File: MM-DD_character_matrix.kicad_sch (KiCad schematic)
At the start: 17 parts, among them U10 SM411006N/15, U11 SN74LVC244A, U12 SM411006N/15, U13 SM411006N/15, U14 SM411006N/15, U8 SN74LVC244A, U9 SM411006N/15

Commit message: verification
- sensor schematic verification
- change in the value of current limiting resistor
- disconnected unused buffer pins
- labeling or peripherals used in primary MCU
- additional user button
- DRC corrections
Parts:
- R10, R44, R45, R46, R6, R7, R8, R9: value 20R -> 10R
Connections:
- net GND: no longer U11.5 (2Y1), U11.7 (2Y2), U11.9 (2Y3)
- no-connect marks 0 -> 3
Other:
- company: Rajath Katker -> TJ71PL
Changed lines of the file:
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@@
 	(title_block
 		(title "MM-DD Character Matrix & Drivers ")
-		(date "2025-11-04")
+		(date "2025-09-05")
 		(rev "v0.0")
-		(company "Rajath Katker")
+		(company "TJ71PL")
+		(comment 1 "天計")
 		(comment 4 "Final verification pending")
 	)
@@
 	(text "MM-DD Character matrix"
 		(exclude_from_sim no)
-		(at 17.78 95.25 0)
+		(at 16.51 96.52 0)
 		(effects
 			(font
@@
 	(text "MM-DD Character matrix drivers "
 		(exclude_from_sim no)
-		(at 16.51 191.77 0)
+		(at 15.24 193.548 0)
 		(effects
 			(font
@@
 	)
 	(junction
-		(at 161.29 152.4)
-		(diameter 0)
-		(color 0 0 0 0)
-	)
-	(junction
-		(at 161.29 154.94)
-		(diameter 0)
-		(color 0 0 0 0)
-	)
-	(junction
 		(at 130.81 152.4)
 		(diameter 0)
@@
 		(color 0 0 0 0)
 	)
+	(no_connect
+		(at 158.75 154.94)
+	)
+	(no_connect
+		(at 158.75 149.86)
+	)
+	(no_connect
+		(at 158.75 152.4)
+	)
 	(bus_entry
 		(at 168.91 134.62)
@@
 	(wire
 		(pts
-			(xy 161.29 149.86) (xy 161.29 152.4)
-		)
-		(stroke
-			(width 0)
-			(type default)
-		)
-	)
-	(wire
-		(pts
 			(xy 158.75 147.32) (xy 166.37 147.32)
 		)
@@
 		)
 	)
-	(wire
-		(pts
-			(xy 161.29 172.72) (xy 146.05 172.72)
-		)
-		(stroke
-			(width 0)
-			(type default)
-		)
-	)
 	(bus
 		(pts
@@
 	(wire
 		(pts
-			(xy 161.29 154.94) (xy 161.29 172.72)
-		)
-		(stroke
-			(width 0)
-			(type default)
-		)
-	)
-	(wire
-		(pts
 			(xy 130.81 152.4) (xy 133.35 152.4)
 		)
@@
 	(wire
 		(pts
-			(xy 158.75 154.94) (xy 161.29 154.94)
-		)
-		(stroke
-			(width 0)
-			(type default)
-		)
-	)
-	(wire
-		(pts
 			(xy 91.44 149.86) (xy 99.06 149.86)
 		)
@@
 		)
 	)
-	(wire
-		(pts
-			(xy 158.75 149.86) (xy 161.29 149.86)
-		)
-		(stroke
-			(width 0)
-			(type default)
-		)
-	)
 	(bus
 		(pts
@@
 		)
 	)
-	(wire
-		(pts
-			(xy 161.29 152.4) (xy 161.29 154.94)
-		)
-		(stroke
-			(width 0)
-			(type default)
-		)
-	)
 	(bus
 		(pts
@@
 		)
 	)
-	(wire
-		(pts
-			(xy 158.75 152.4) (xy 161.29 152.4)
-		)
-		(stroke
-			(width 0)
-			(type default)
-		)
-	)
 	(bus
 		(pts
@@
 			)
 		)
-		(property "Value" "20R"
+		(property "Value" "10R"
 			(at 87.63 170.434 90)
 			(effects
@@
 			)
 		)
-		(property "Value" "20R"
+		(property "Value" "10R"
 			(at 87.63 147.574 90)
 			(effects
@@
 			)
 		)
-		(property "Value" "20R"
+		(property "Value" "10R"
 			(at 87.63 162.814 90)
 			(effects
@@
 			)
 		)
-		(property "Value" "20R"
+		(property "Value" "10R"
 			(at 87.63 155.194 90)
 			(effects
@@
 			)
 		)
-		(property "Value" "20R"
+		(property "Value" "10R"
 			(at 87.63 117.094 90)
 			(effects
@@
 			)
 		)
-		(property "Value" "20R"
+		(property "Value" "10R"
 			(at 87.63 132.334 90)
 			(effects
@@
 			)
 		)
-		(property "Value" "20R"
+		(property "Value" "10R"
 			(at 87.63 124.714 90)
 			(effects
@@
 			)
 		)
-		(property "Value" "20R"
+		(property "Value" "10R"
 			(at 87.63 139.954 90)
 			(effects

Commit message: semi final verification
- change in display type to common cathode
- verification of the schematic
- addition of footprints
- further minor changes
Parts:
- removed U10, U12, U13, U14, U9: SM411006N/15, precision_clock:SM411006N15, symbol precision_clock:SM411006N/15
- added U10, U12, U13, U14, U9: 10016AS, precision_clock:10016AS, symbol precision_clock:10016AS
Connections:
- net BA0: now also R6.2, U10.7 (A), U12.7 (A), U14.7 (A), U9.7 (A); no longer U11.18 (1Y0)
- net BA1: now also R7.2, U10.6 (B), U12.6 (B), U13.6 (B), U13.7 (A), U14.6 (B), U9.6 (B); no longer U11.16 (1Y1)
- net BA2: now also R8.2, U10.4 (C), U12.4 (C), U13.4 (C), U14.4 (C), U9.4 (C); no longer U11.14 (1Y2)
- net BA3: now also R9.2, U10.2 (D), U12.2 (D), U13.2 (D), U14.2 (D), U9.2 (D); no longer U11.12 (1Y3)
- net BA4: now also R10.2, U10.1 (E), U12.1 (E), U13.1 (E), U14.1 (E), U9.1 (E); no longer U11.3 (2Y0)
- net BK0: now also U11.18 (1Y0), U9.3 (CK), U9.8 (CK); no longer R6.2
- net BK1: now also U11.16 (1Y1), U10.3 (CK), U10.8 (CK); no longer R7.2
- net BK2: now also U11.14 (1Y2), U12.3 (CK), U12.8 (CK); no longer R8.2
- net BK3: now also U11.12 (1Y3), U13.3 (CK), U13.8 (CK); no longer R9.2
- net BK4: now also U11.3 (2Y0), U14.3 (CK), U14.8 (CK); no longer R10.2
- net M2A0: now also U8.2 (1A0); no longer U11.2 (1A0)
- net M2A1: now also U8.4 (1A1); no longer U11.4 (1A1)
- net M2A2: now also U8.6 (1A2); no longer U11.6 (1A2)
- net M2A3: now also U8.8 (1A3); no longer U11.8 (1A3)
- net M2A4: now also U8.17 (2A0); no longer U11.17 (2A0)
- net M2K0: now also U11.2 (1A0); no longer U8.2 (1A0)
- net M2K1: now also U11.4 (1A1); no longer U8.4 (1A1)
- net M2K2: now also U11.6 (1A2); no longer U8.6 (1A2)
- net M2K3: now also U11.8 (1A3); no longer U8.8 (1A3)
- net M2K4: now also U11.17 (2A0); no longer U8.17 (2A0)
- net BK5 renamed BA5
- net BA5: now also U10.9 (F), U12.9 (F), U13.9 (F), U14.9 (F), U9.9 (F)
- net BK6 renamed BA6
- net BA6: now also U10.10 (G), U12.10 (G), U13.10 (G), U14.10 (G), U9.10 (G)
- net BK7 renamed BA7
- net BA7: now also U10.5 (DP), U12.5 (DP), U13.5 (DP), U14.5 (DP), U9.5 (DP)
- net M2K5 renamed M2A5
- net M2K6 renamed M2A6
- net M2K7 renamed M2A7

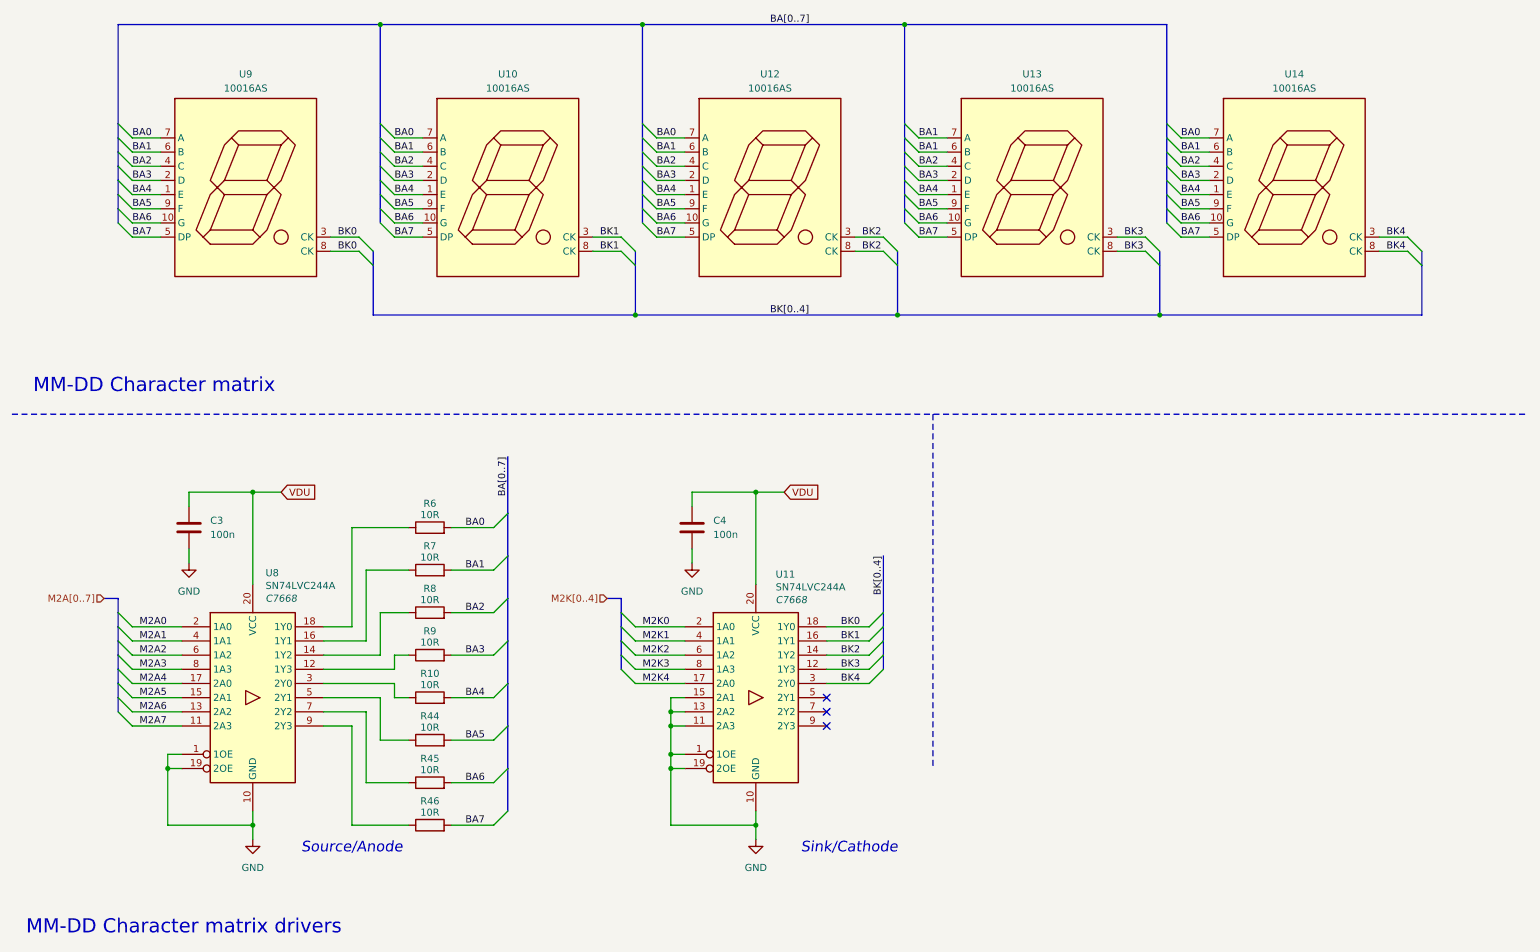
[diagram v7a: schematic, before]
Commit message: PCB routing
- JLCPCB constraints added
- removal of multiple test points
- change of footprints
- change of THT LEDs
- rough position of all the major components
- PCB routing started
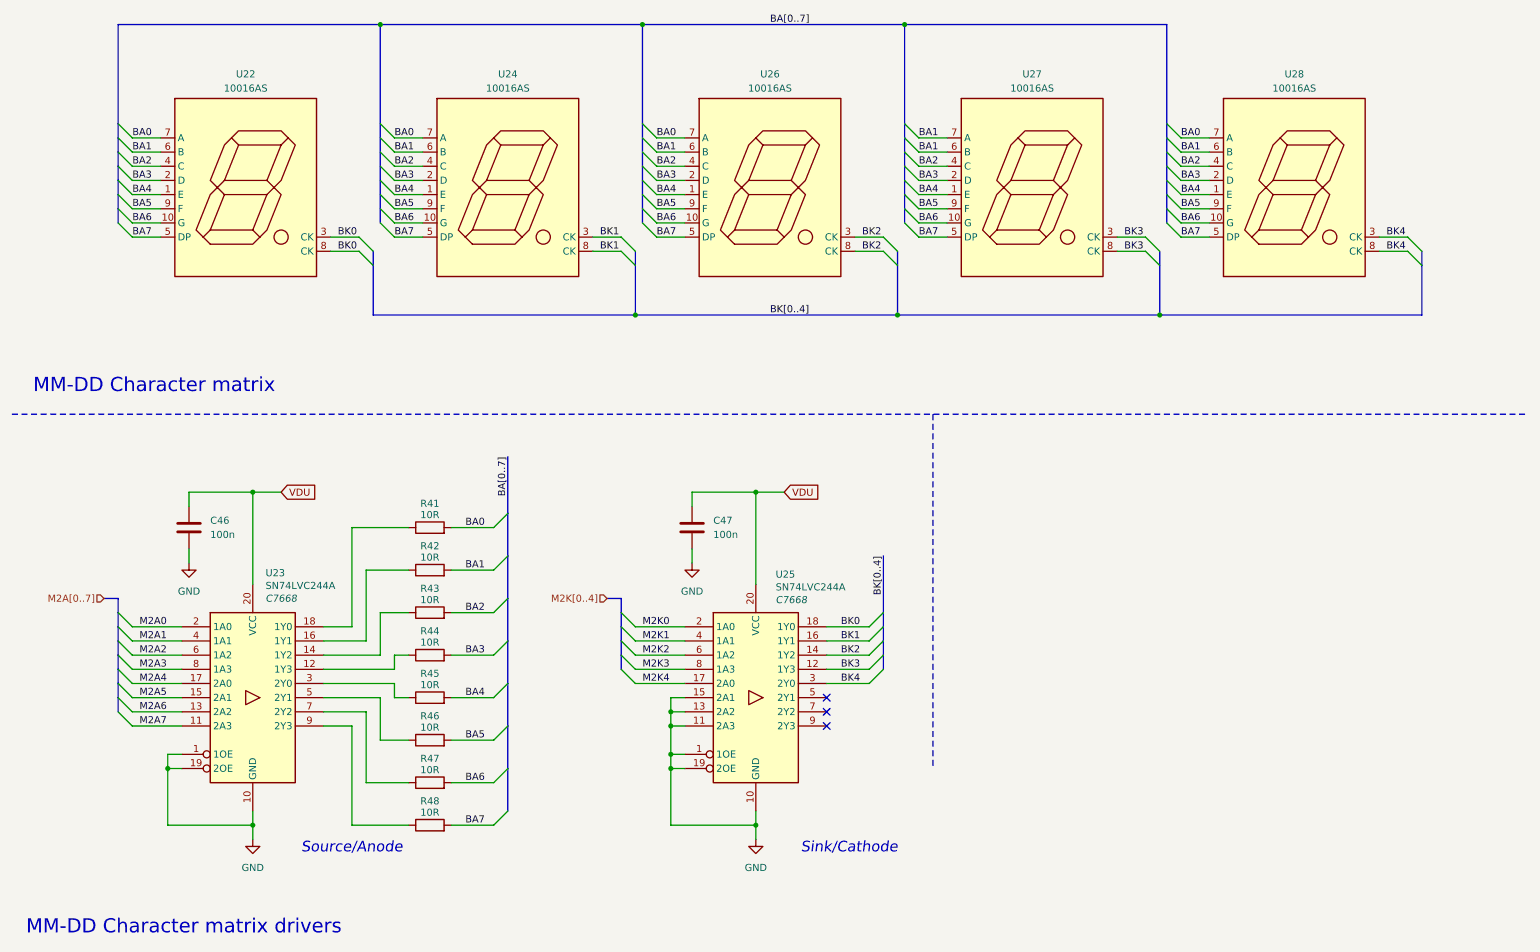
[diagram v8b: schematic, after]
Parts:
- U22: renamed from U9; footprint precision_clock:10016AS -> precision_clock:Xlitx 10016AS
- U24: renamed from U10; footprint precision_clock:10016AS -> precision_clock:Xlitx 10016AS
- U26: renamed from U12; footprint precision_clock:10016AS -> precision_clock:Xlitx 10016AS
- U27: renamed from U13; footprint precision_clock:10016AS -> precision_clock:Xlitx 10016AS
- U28: renamed from U14; footprint precision_clock:10016AS -> precision_clock:Xlitx 10016AS
- renumbered C3 to C46, C4 to C47, R6 to R41, R7 to R42, R8 to R43, R9 to R44, R10 to R45, R44 to R46, R45 to R47, R46 to R48, U8 to U23, U11 to U25
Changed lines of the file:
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@@
 		(on_board yes)
 		(dnp no)
-		(property "Reference" "U8"
+		(property "Reference" "U23"
 			(at 58.166 130.048 0)
 			(effects
@@
 			(project "Precision Clock"
 				(path "/c9a8ff63-a0d1-4125-9dd1-40fb53daf536/e0daf664-e239-498f-ad2e-96c4213a6fbd"
-					(reference "U8")
+					(reference "U23")
 					(unit 1)
 				)
@@
 		(on_board yes)
 		(dnp no)
-		(property "Reference" "R44"
+		(property "Reference" "R46"
 			(at 87.63 155.702 90)
 			(effects
@@
 			(project "Precision Clock"
 				(path "/c9a8ff63-a0d1-4125-9dd1-40fb53daf536/e0daf664-e239-498f-ad2e-96c4213a6fbd"
-					(reference "R44")
+					(reference "R46")
 					(unit 1)
 				)
@@
 		(dnp no)
 		(fields_autoplaced yes)
-		(property "Reference" "C3"
+		(property "Reference" "C46"
 			(at 48.26 120.6499 0)
 			(effects
@@
 			(project "Precision Clock"
 				(path "/c9a8ff63-a0d1-4125-9dd1-40fb53daf536/e0daf664-e239-498f-ad2e-96c4213a6fbd"
-					(reference "C3")
+					(reference "C46")
 					(unit 1)
 				)
@@
 		(dnp no)
 		(fields_autoplaced yes)
-		(property "Reference" "#PWR08"
+		(property "Reference" "#PWR0107"
 			(at 146.05 184.15 0)
 			(effects
@@
 			(project "Precision Clock"
 				(path "/c9a8ff63-a0d1-4125-9dd1-40fb53daf536/e0daf664-e239-498f-ad2e-96c4213a6fbd"
-					(reference "#PWR08")
+					(reference "#PWR0107")
 					(unit 1)
 				)
@@
 		(dnp no)
 		(fields_autoplaced yes)
-		(property "Reference" "U14"
+		(property "Reference" "U28"
 			(at 242.57 40.64 0)
 			(effects
@@
 			)
 		)
-		(property "Footprint" "precision_clock:10016AS"
+		(property "Footprint" "precision_clock:Xlitx 10016AS"
 			(at 242.57 60.96 0)
 			(effects
@@
 			(project "Precision Clock"
 				(path "/c9a8ff63-a0d1-4125-9dd1-40fb53daf536/e0daf664-e239-498f-ad2e-96c4213a6fbd"
-					(reference "U14")
+					(reference "U28")
 					(unit 1)
 				)
@@
 		(on_board yes)
 		(dnp no)
-		(property "Reference" "R10"
+		(property "Reference" "R45"
 			(at 87.63 148.082 90)
 			(effects
@@
 			(project "Precision Clock"
 				(path "/c9a8ff63-a0d1-4125-9dd1-40fb53daf536/e0daf664-e239-498f-ad2e-96c4213a6fbd"
-					(reference "R10")
+					(reference "R45")
 					(unit 1)
 				)
@@
 		(on_board yes)
 		(dnp no)
-		(property "Reference" "R7"
+		(property "Reference" "R42"
 			(at 87.63 125.222 90)
 			(effects
@@
 			(project "Precision Clock"
 				(path "/c9a8ff63-a0d1-4125-9dd1-40fb53daf536/e0daf664-e239-498f-ad2e-96c4213a6fbd"
-					(reference "R7")
+					(reference "R42")
 					(unit 1)
 				)
@@
 		(dnp no)
 		(fields_autoplaced yes)
-		(property "Reference" "#PWR07"
+		(property "Reference" "#PWR0106"
 			(at 134.62 134.62 0)
 			(effects
@@
 			(project "Precision Clock"
 				(path "/c9a8ff63-a0d1-4125-9dd1-40fb53daf536/e0daf664-e239-498f-ad2e-96c4213a6fbd"
-					(reference "#PWR07")
+					(reference "#PWR0106")
 					(unit 1)
 				)
@@
 		(dnp no)
 		(fields_autoplaced yes)
-		(property "Reference" "U9"
+		(property "Reference" "U22"
 			(at 54.61 40.64 0)
 			(effects
@@
 			)
 		)
-		(property "Footprint" "precision_clock:10016AS"
+		(property "Footprint" "precision_clock:Xlitx 10016AS"
 			(at 54.61 60.96 0)
 			(effects
@@
 			(project "Precision Clock"
 				(path "/c9a8ff63-a0d1-4125-9dd1-40fb53daf536/e0daf664-e239-498f-ad2e-96c4213a6fbd"
-					(reference "U9")
+					(reference "U22")
 					(unit 1)
 				)
@@
 		(dnp no)
 		(fields_autoplaced yes)
-		(property "Reference" "U13"
+		(property "Reference" "U27"
 			(at 195.58 40.64 0)
 			(effects
@@
 			)
 		)
-		(property "Footprint" "precision_clock:10016AS"
+		(property "Footprint" "precision_clock:Xlitx 10016AS"
 			(at 195.58 60.96 0)
 			(effects
@@
 			(project "Precision Clock"
 				(path "/c9a8ff63-a0d1-4125-9dd1-40fb53daf536/e0daf664-e239-498f-ad2e-96c4213a6fbd"
-					(reference "U13")
+					(reference "U27")
 					(unit 1)
 				)
@@
 		(dnp no)
 		(fields_autoplaced yes)
-		(property "Reference" "U12"
+		(property "Reference" "U26"
 			(at 148.59 40.64 0)
 			(effects
@@
 			)
 		)
-		(property "Footprint" "precision_clock:10016AS"
+		(property "Footprint" "precision_clock:Xlitx 10016AS"
 			(at 148.59 60.96 0)
 			(effects
@@
 			(project "Precision Clock"
 				(path "/c9a8ff63-a0d1-4125-9dd1-40fb53daf536/e0daf664-e239-498f-ad2e-96c4213a6fbd"
-					(reference "U12")
+					(reference "U26")
 					(unit 1)
 				)
@@
 		(dnp no)
 		(fields_autoplaced yes)
-		(property "Reference" "#PWR05"
+		(property "Reference" "#PWR0104"
 			(at 44.45 134.62 0)
 			(effects
@@
 			(project "Precision Clock"
 				(path "/c9a8ff63-a0d1-4125-9dd1-40fb53daf536/e0daf664-e239-498f-ad2e-96c4213a6fbd"
-					(reference "#PWR05")
+					(reference "#PWR0104")
 					(unit 1)
 				)
@@
 		(on_board yes)
 		(dnp no)
-		(property "Reference" "U11"
+		(property "Reference" "U25"
 			(at 149.606 130.302 0)
 			(effects
@@
 			(project "Precision Clock"
 				(path "/c9a8ff63-a0d1-4125-9dd1-40fb53daf536/e0daf664-e239-498f-ad2e-96c4213a6fbd"
-					(reference "U11")
+					(reference "U25")
 					(unit 1)
 				)
@@
 		(on_board yes)
 		(dnp no)
-		(property "Reference" "R46"
+		(property "Reference" "R48"
 			(at 87.63 170.942 90)
 			(effects
@@
 			(project "Precision Clock"
 				(path "/c9a8ff63-a0d1-4125-9dd1-40fb53daf536/e0daf664-e239-498f-ad2e-96c4213a6fbd"
-					(reference "R46")
+					(reference "R48")
 					(unit 1)
 				)
@@
 		(dnp no)
 		(fields_autoplaced yes)
-		(property "Reference" "#PWR06"
+		(property "Reference" "#PWR0105"
 			(at 55.88 184.15 0)
 			(effects
@@
 			(project "Precision Clock"
 				(path "/c9a8ff63-a0d1-4125-9dd1-40fb53daf536/e0daf664-e239-498f-ad2e-96c4213a6fbd"
-					(reference "#PWR06")
+					(reference "#PWR0105")
 					(unit 1)
 				)
@@
 		(on_board yes)
 		(dnp no)
-		(property "Reference" "R45"
+		(property "Reference" "R47"
 			(at 87.63 163.322 90)
 			(effects
@@
 			(project "Precision Clock"
 				(path "/c9a8ff63-a0d1-4125-9dd1-40fb53daf536/e0daf664-e239-498f-ad2e-96c4213a6fbd"
-					(reference "R45")
+					(reference "R47")
 					(unit 1)
 				)
@@
 		(on_board yes)
 		(dnp no)
-		(property "Reference" "R9"
+		(property "Reference" "R44"
 			(at 87.63 140.462 90)
 			(effects
@@
 			(project "Precision Clock"
 				(path "/c9a8ff63-a0d1-4125-9dd1-40fb53daf536/e0daf664-e239-498f-ad2e-96c4213a6fbd"
-					(reference "R9")
+					(reference "R44")
 					(unit 1)
 				)
@@
 		(on_board yes)
 		(dnp no)
-		(property "Reference" "R8"
+		(property "Reference" "R43"
 			(at 87.63 132.842 90)
 			(effects
@@
 			(project "Precision Clock"
 				(path "/c9a8ff63-a0d1-4125-9dd1-40fb53daf536/e0daf664-e239-498f-ad2e-96c4213a6fbd"
-					(reference "R8")
+					(reference "R43")
 					(unit 1)
 				)
@@
 		(dnp no)
 		(fields_autoplaced yes)
-		(property "Reference" "C4"
+		(property "Reference" "C47"
 			(at 138.43 120.6499 0)
 			(effects
@@
 			(project "Precision Clock"
 				(path "/c9a8ff63-a0d1-4125-9dd1-40fb53daf536/e0daf664-e239-498f-ad2e-96c4213a6fbd"
-					(reference "C4")
+					(reference "C47")
 					(unit 1)
 				)
@@
 		(on_board yes)
 		(dnp no)
-		(property "Reference" "R6"
+		(property "Reference" "R41"
 			(at 87.63 117.602 90)
 			(effects
@@
 			(project "Precision Clock"
 				(path "/c9a8ff63-a0d1-4125-9dd1-40fb53daf536/e0daf664-e239-498f-ad2e-96c4213a6fbd"
-					(reference "R6")
+					(reference "R41")
 					(unit 1)
 				)
@@
 		(dnp no)
 		(fields_autoplaced yes)
-		(property "Reference" "U10"
+		(property "Reference" "U24"
 			(at 101.6 40.64 0)
 			(effects
@@
 			)
 		)
-		(property "Footprint" "precision_clock:10016AS"
+		(property "Footprint" "precision_clock:Xlitx 10016AS"
 			(at 101.6 60.96 0)
 			(effects
@@
 			(project "Precision Clock"
 				(path "/c9a8ff63-a0d1-4125-9dd1-40fb53daf536/e0daf664-e239-498f-ad2e-96c4213a6fbd"
-					(reference "U10")
-					(unit 1)
-				)
+					(reference "U24")
+					(unit 1)
+				)
